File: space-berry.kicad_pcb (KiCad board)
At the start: 6 copper layers, 97 parts, among them J1 ARJM11C7-502-AB-ER2-T, Q1 SiS415DNT, Q2 TSM2302CX, U11 RTL8211F-CG, U12 K4A8G165WC-BCTD, U13 XCZU15EG-2FFVB1156E, U6 TLV75801PDBV, U7 TLV75801PDBV, U8 TLV75801PDBV, U9 TLV75801PDBV

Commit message: Stuff
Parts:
- removed J1: ARJM11C7-502-AB-ER2-T, lib:ARJM11C7-502-AB-ER2-T_ABR
- added R20: 22, Resistor_SMD:R_0402_1005Metric_Pad0.72x0.64mm_HandSolder, F.Cu at (61.6, 86.6)
- added R33: 22, Resistor_SMD:R_0402_1005Metric_Pad0.72x0.64mm_HandSolder, F.Cu at (61.6, 88.6)
- added R34: 22, Resistor_SMD:R_0402_1005Metric_Pad0.72x0.64mm_HandSolder, F.Cu at (61.6, 90.6)
- added R35: 22, Resistor_SMD:R_0402_1005Metric_Pad0.72x0.64mm_HandSolder, F.Cu at (61.6, 92.6)
- added R36: 4K7, Resistor_SMD:R_0402_1005Metric_Pad0.72x0.64mm_HandSolder, F.Cu at (61.6, 94.5)
- added R37: 4K7, Resistor_SMD:R_0402_1005Metric_Pad0.72x0.64mm_HandSolder, F.Cu at (61.6, 96.5)
- added R38: 4K7, Resistor_SMD:R_0402_1005Metric_Pad0.72x0.64mm_HandSolder, F.Cu at (64.8, 86.6)
- added R39: 4K7, Resistor_SMD:R_0402_1005Metric_Pad0.72x0.64mm_HandSolder, F.Cu at (64.8, 88.6)
- added R41: 4K7, Resistor_SMD:R_0402_1005Metric_Pad0.72x0.64mm_HandSolder, F.Cu at (64.8, 90.6)
- added R42: 4K7, Resistor_SMD:R_0402_1005Metric_Pad0.72x0.64mm_HandSolder, F.Cu at (64.8, 92.6)
- added R43: 4K7, Resistor_SMD:R_0402_1005Metric_Pad0.72x0.64mm_HandSolder, F.Cu at (64.8, 94.5)
- added R44: 4K7, Resistor_SMD:R_0402_1005Metric_Pad0.72x0.64mm_HandSolder, F.Cu at (64.8, 96.5)
- added R45: 22, Resistor_SMD:R_0402_1005Metric_Pad0.72x0.64mm_HandSolder, F.Cu at (68.1, 86.6)
- added R46: 22, Resistor_SMD:R_0402_1005Metric_Pad0.72x0.64mm_HandSolder, F.Cu at (68.1, 88.6)
- added R47: 22, Resistor_SMD:R_0402_1005Metric_Pad0.72x0.64mm_HandSolder, F.Cu at (68.1, 90.6)
- added R48: 22, Resistor_SMD:R_0402_1005Metric_Pad0.72x0.64mm_HandSolder, F.Cu at (68.1, 92.6)
- moved U11 9.92 mm to (73.5, 89.4)
- moved U12 8.24 mm to (136.8, 74.9)
- moved R23 5.93 mm to (154.8, 48.0), turned to 90 degrees
- moved R24 5.93 mm to (152.0, 53.2), turned to 0 degrees
- moved C28 4.25 mm to (118.4, 56.9), turned to -90 degrees
- moved R19 3.77 mm to (146.0, 74.8), turned to 90 degrees
- moved R27 2.02 mm to (116.9, 54.2), turned to 180 degrees
- moved R28 1.28 mm to (113.2, 54.2)
- moved C27 1.28 mm to (112.0, 56.9)
- moved U9 1.28 mm to (115.2, 56.9)
- moved U13 0.99 mm to (108.0, 81.1)
- turned C24 to -90 degrees
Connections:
- U11 pad 1: unconnected-(U11A-MDIP0-Pad1) -> ETH_TR1+
- U11 pad 10: unconnected-(U11A-MDIN3-Pad10) -> ETH_TR4-
- U11 pad 11: unconnected-(U11B-AVDD33-Pad11) -> (no net)
- U11 pad 15: unconnected-(U11A-TXD3-Pad15) -> Net-(U11A-TXD3)
- U11 pad 16: unconnected-(U11A-TXD2-Pad16) -> Net-(U11A-TXD2)
- U11 pad 17: unconnected-(U11A-TXD1-Pad17) -> Net-(U11A-TXD1)
- U11 pad 18: unconnected-(U11A-TXD0-Pad18) -> Net-(U11A-TXD0)
- U11 pad 2: unconnected-(U11A-MDIN0-Pad2) -> ETH_TR1-
- U11 pad 21: unconnected-(U11B-DVDD10-Pad21) -> (no net)
- U11 pad 22: unconnected-(U11A-RXD3/PHYAD0-Pad22) -> Net-(U11A-RXD3/PHYAD0)
- U11 pad 23: unconnected-(U11A-RXD2/PLLOFF-Pad23) -> Net-(U11A-RXD2/PLLOFF)
- U11 pad 24: unconnected-(U11A-RXD1/TXDLY-Pad24) -> Net-(U11A-RXD1/TXDLY)
- U11 pad 25: unconnected-(U11A-RXD0/RXDLY-Pad25) -> Net-(U11A-RXD0/RXDLY)
- U11 pad 28: unconnected-(U11B-DVDD_RG-Pad28) -> (no net)
- U11 pad 29: unconnected-(U11B-DVDD33-Pad29) -> (no net)
- U11 pad 3: unconnected-(U11B-AVDD10-Pad3) -> (no net)
- U11 pad 38: unconnected-(U11B-AVDD10-Pad38) -> (no net)
- U11 pad 4: unconnected-(U11A-MDIP1-Pad4) -> ETH_TR2+
- U11 pad 40: unconnected-(U11B-AVDD33-Pad40) -> (no net)
- U11 pad 41: unconnected-(U11B-GND-Pad41) -> (no net)
- U11 pad 5: unconnected-(U11A-MDIN1-Pad5) -> ETH_TR2-
- U11 pad 6: unconnected-(U11A-MDIP2-Pad6) -> ETH_TR3+
- U11 pad 7: unconnected-(U11A-MDIN2-Pad7) -> ETH_TR3-
- U11 pad 8: unconnected-(U11B-AVDD10-Pad8) -> (no net)
- U11 pad 9: unconnected-(U11A-MDIP3-Pad9) -> ETH_TR4+
- U13 pad A1: (no net) -> Net-(U13P-GND-PadA1)
- U13 pad A10: (no net) -> Net-(U13M-MGTAVCC_R-PadA10)
- U13 pad A2: (no net) -> Net-(U13P-GND-PadA1)
- U13 pad A30: (no net) -> unconnected-(U13M-MGTAVTTRCAL_L-PadA30)
- U13 pad A5: (no net) -> unconnected-(U13M-MGTAVTTRCAL_R-PadA5)
- U13 pad A9: (no net) -> Net-(U13P-GND-PadA1)
- U13 pad AA13: (no net) -> Net-(U13O-VCCINT_IO-PadAA13)
- U13 pad AA15: (no net) -> VCC_INT
- U13 pad AA17: (no net) -> VCC_INT
- U13 pad AA19: (no net) -> VCC_INT
- U13 pad AA21: (no net) -> Net-(U13N-VCC_PSINTLP-PadAA21)
- U13 pad AA22: (no net) -> unconnected-(U13N-VCC_PSBATT-PadAA22)
- U13 pad AA23: (no net) -> Net-(U13N-VCC_PSADC-PadAB25)
- U13 pad AA25: (no net) -> Net-(U13N-VCC_PSADC-PadAB25)
- U13 pad AA29: (no net) -> Net-(U13N-PS_MGTRAVCC-PadAA29)
- U13 pad AA9: (no net) -> unconnected-(U13P-VCCO_66-PadAA9)
- U13 pad AB13: (no net) -> Net-(U13O-VCCINT_IO-PadAA13)
- U13 pad AB14: (no net) -> Net-(U13N-VCCBRAM-PadAB14)
- U13 pad AB16: (no net) -> VCC_INT
- U13 pad AB18: (no net) -> VCC_INT
- U13 pad AB20: (no net) -> VCC_INT
- U13 pad AB21: (no net) -> Net-(U13N-VCC_PSINTLP-PadAA21)
- U13 pad AB23: (no net) -> Net-(U13N-VCC_PSINTLP-PadAA21)
- U13 pad AB25: (no net) -> Net-(U13N-VCC_PSADC-PadAB25)
- U13 pad AB32: (no net) -> Net-(U13N-PS_MGTRAVTT-PadAB32)
- U13 pad AC13: (no net) -> Net-(U13O-VCCINT_IO-PadAA13)
- U13 pad AC14: (no net) -> Net-(U13N-VCCBRAM-PadAB14)
- U13 pad AC15: (no net) -> VCC_INT
- U13 pad AC17: (no net) -> VCC_INT
- U13 pad AC19: (no net) -> VCC_INT
- U13 pad AC21: (no net) -> Net-(U13N-VCC_PSINTLP-PadAA21)
- U13 pad AC22: (no net) -> Net-(U13N-VCC_PSINTLP-PadAA21)
- U13 pad AC23: (no net) -> Net-(U13N-VCC_PSINTLP-PadAA21)
- U13 pad AC24: (no net) -> Net-(U13N-VCC_PSINTFP-PadAC24)
- U13 pad AC26: (no net) -> Net-(U13N-VCC_PSADC-PadAB25)
- U13 pad AD11: (no net) -> unconnected-(U13P-VREF_65-PadAD11)
- U13 pad AD12: (no net) -> unconnected-(U13P-VREF_66-PadAD12)
- U13 pad AD17: unconnected-(U13K-PS_MIO7-PadAD17) -> UART0_TX
- U13 pad AD18: unconnected-(U13K-PS_MIO20-PadAD18) -> SD_DATA7
- U13 pad AD20: unconnected-(U13K-PS_MIO22-PadAD20) -> SD_CLK
- U13 pad AD21: (no net) -> Net-(U13N-VCC_PSINTFP-PadAC24)
- U13 pad AD22: (no net) -> Net-(U13N-VCC_PSINTFP-PadAC24)
- U13 pad AD24: (no net) -> Net-(U13N-VCC_PSINTFP_DDR-PadAD24)
- U13 pad AD25: (no net) -> Net-(U13N-VCC_PSINTFP-PadAC24)
- U13 pad AD26: (no net) -> Net-(U13N-VCC_PSINTFP-PadAC24)
- U13 pad AD8: (no net) -> unconnected-(U13P-VCCO_65-PadAD8)
- U13 pad AE16: (no net) -> Net-(U13P-VCCO_PSIO0_500-PadAE16)
- U13 pad AE17: unconnected-(U13K-PS_MIO8-PadAE17) -> UART1_RX
- U13 pad AE18: unconnected-(U13K-PS_MIO18-PadAE18) -> SD_DATA5
- U13 pad AE22: (no net) -> Net-(U13N-VCC_PSINTFP-PadAC24)
- U13 pad AE23: (no net) -> Net-(U13N-VCC_PSINTFP-PadAC24)
- U13 pad AE24: (no net) -> Net-(U13N-VCC_PSINTFP_DDR-PadAD24)
- U13 pad AE25: (no net) -> Net-(U13N-VCC_PSINTFP_DDR-PadAD24)
- U13 pad AF14: (no net) -> unconnected-(U13P-VCCO_44-PadAF14)
- U13 pad AF18: unconnected-(U13K-PS_MIO21-PadAF18) -> SD_CMD
- U13 pad AF26: (no net) -> unconnected-(U13M-NC-PadAF26)
- U13 pad AF27: (no net) -> unconnected-(U13M-NC-PadAF27)
- U13 pad AF9: (no net) -> unconnected-(U13P-VCCO_65-PadAF9)
- U13 pad AG17: (no net) -> Net-(U13P-VCCO_PSIO0_500-PadAE16)
- U13 pad AG27: (no net) -> Net-(U13P-VCCO_PSDDR_504-PadAG27)
- U13 pad AG7: (no net) -> unconnected-(U13P-VCCO_65-PadAG7)
- U13 pad AJ11: (no net) -> unconnected-(U13P-VREF_64-PadAJ11)
- U13 pad AJ13: (no net) -> unconnected-(U13P-VCCO_44-PadAJ13)
- U13 pad AJ24: (no net) -> Net-(U13P-VCCO_PSDDR_504-PadAG27)
- U13 pad AJ28: (no net) -> Net-(U13P-VCCO_PSDDR_504-PadAG27)
- U13 pad AJ8: (no net) -> unconnected-(U13P-VCCO_64-PadAJ8)
- U13 pad AK11: (no net) -> unconnected-(U13P-VCCO_64-PadAK11)
- U13 pad AK16: (no net) -> Net-(U13P-VCCO_PSIO0_500-PadAE16)
- U13 pad AK17: unconnected-(U13K-PS_MIO13-PadAK17) -> SD_DATA0
- U13 pad AL15: unconnected-(U13K-PS_MIO6-PadAL15) -> UART0_RX
- U13 pad AL16: unconnected-(U13K-PS_MIO14-PadAL16) -> SD_DATA1
- U13 pad AL17: unconnected-(U13K-PS_MIO19-PadAL17) -> SD_DATA6
- U13 pad AL24: (no net) -> Net-(U13P-VCCO_PSDDR_504-PadAG27)
- U13 pad AL29: (no net) -> Net-(U13P-VCCO_PSDDR_504-PadAG27)
- U13 pad AL9: (no net) -> unconnected-(U13P-VCCO_64-PadAL9)
- U13 pad AM16: unconnected-(U13K-PS_MIO16-PadAM16) -> SD_DATA3
- U13 pad AN16: unconnected-(U13K-PS_MIO15-PadAN16) -> SD_DATA2
- U13 pad AN25: (no net) -> Net-(U13P-VCCO_PSDDR_504-PadAG27)
- U13 pad AN30: (no net) -> Net-(U13P-VCCO_PSDDR_504-PadAG27)
- U13 pad AP15: unconnected-(U13K-PS_MIO9-PadAP15) -> UART1_TX
- U13 pad AP16: unconnected-(U13K-PS_MIO17-PadAP16) -> SD_DATA4
- U13 pad B3: (no net) -> Net-(U13M-MGTAVTT_R-PadB3)
- U13 pad B31: (no net) -> Net-(U13M-MGTAVTT_L-PadB31)
- U13 pad B4: (no net) -> Net-(U13P-GND-PadA1)
- U13 pad B8: (no net) -> Net-(U13M-MGTAVCC_R-PadA10)
- U13 pad C29: (no net) -> Net-(U13M-MGTAVTT_L-PadB31)
- U13 pad C6: (no net) -> Net-(U13M-MGTAVCC_R-PadA10)
- U13 pad D23: (no net) -> Net-(U13P-VCCO_PSIO2_502-PadD23)
- U13 pad D32: (no net) -> Net-(U13M-MGTAVTT_L-PadB31)
- U13 pad D4: (no net) -> Net-(U13M-MGTAVTT_R-PadB3)
- U13 pad D7: (no net) -> Net-(U13M-MGTAVCC_R-PadA10)
- U13 pad E16: (no net) -> unconnected-(U13P-VCCO_49-PadE16)
- U13 pad E21: (no net) -> unconnected-(U13P-VCCO_47-PadE21)
- U13 pad E30: (no net) -> Net-(U13M-MGTAVTT_L-PadB31)
- U13 pad E5: (no net) -> Net-(U13M-MGTAVCC_R-PadA10)
- U13 pad F14: (no net) -> unconnected-(U13P-VCCO_49-PadF14)
- U13 pad F24: (no net) -> Net-(U13P-VCCO_PSIO2_502-PadD23)
- U13 pad F28: (no net) -> Net-(U13M-MGTAVCC_L-PadF28)
- U13 pad F3: (no net) -> Net-(U13M-MGTAVTT_R-PadB3)
- U13 pad F31: (no net) -> Net-(U13M-MGTAVTT_L-PadB31)
- U13 pad F8: (no net) -> Net-(U13M-MGTVCCAUX_R-PadF8)
- U13 pad G12: (no net) -> unconnected-(U13P-VCCO_50-PadG12)
- U13 pad G17: (no net) -> unconnected-(U13P-VCCO_48-PadG17)
- U13 pad G22: (no net) -> Net-(U13P-VCCO_PSIO2_502-PadD23)
- U13 pad G29: (no net) -> Net-(U13M-MGTAVCC_L-PadF28)
- U13 pad G6: (no net) -> Net-(U13M-MGTAVCC_R-PadA10)
- U13 pad H20: (no net) -> unconnected-(U13P-VCCO_47-PadH20)
- U13 pad H27: (no net) -> Net-(U13M-MGTAVCC_L-PadF28)
- U13 pad H32: (no net) -> Net-(U13M-MGTAVTT_L-PadB31)
- U13 pad H4: (no net) -> Net-(U13M-MGTAVTT_R-PadB3)
- U13 pad H7: (no net) -> Net-(U13M-MGTVCCAUX_R-PadF8)
- U13 pad J13: (no net) -> unconnected-(U13P-VCCO_50-PadJ13)
- U13 pad J18: (no net) -> unconnected-(U13P-VCCO_48-PadJ18)
- U13 pad J24: unconnected-(U13K-PS_MIO41-PadJ24) -> ETH_TXD2
- U13 pad J25: unconnected-(U13K-PS_MIO46-PadJ25) -> ETH_RXD3
- U13 pad J30: (no net) -> Net-(U13M-MGTAVTT_L-PadB31)
- U13 pad J5: (no net) -> Net-(U13M-MGTAVTT_R-PadB3)
- U13 pad K24: unconnected-(U13K-PS_MIO43-PadK24) -> ETH_RXD0
- U13 pad K28: (no net) -> Net-(U13M-MGTVCCAUX_L-PadK28)
- U13 pad K3: (no net) -> Net-(U13M-MGTAVTT_R-PadB3)
- U13 pad K31: (no net) -> Net-(U13M-MGTAVTT_L-PadB31)
- U13 pad K8: (no net) -> Net-(U13M-MGTAVCC_R-PadA10)
- U13 pad L23: unconnected-(U13K-PS_MIO38-PadL23) -> ETH_CLK
- U13 pad L24: (no net) -> Net-(U13P-VCCO_PSIO1_501-PadL24)
- U13 pad L29: (no net) -> Net-(U13M-MGTAVCC_L-PadF28)
- U13 pad L6: (no net) -> Net-(U13M-MGTAVTT_R-PadB3)
- U13 pad M16: (no net) -> VCC_INT
- U13 pad M18: (no net) -> VCC_INT
- U13 pad M20: (no net) -> VCC_INT
- U13 pad M22: (no net) -> Net-(U13P-VCCO_PSIO1_501-PadL24)
- U13 pad M23: unconnected-(U13K-PS_MIO40-PadM23) -> ETH_TXD1
- U13 pad M24: unconnected-(U13K-PS_MIO42-PadM24) -> ETH_TXD3
- U13 pad M27: (no net) -> Net-(U13M-MGTVCCAUX_L-PadK28)
- U13 pad M32: (no net) -> Net-(U13M-MGTAVTT_L-PadB31)
- U13 pad M4: (no net) -> Net-(U13M-MGTAVTT_R-PadB3)
- U13 pad N14: (no net) -> unconnected-(U13P-VREF_67-PadN14)
- U13 pad N15: (no net) -> VCC_INT
- U13 pad N17: (no net) -> VCC_INT
- U13 pad N19: (no net) -> VCC_INT
- U13 pad N23: unconnected-(U13K-PS_MIO39-PadN23) -> ETH_TXD0
- U13 pad N24: unconnected-(U13K-PS_MIO44-PadN24) -> ETH_RXD1
- U13 pad N30: (no net) -> Net-(U13M-MGTAVTT_L-PadB31)
- U13 pad N5: (no net) -> Net-(U13M-MGTAVTT_R-PadB3)
- U13 pad P14: (no net) -> VCC_INT
- U13 pad P16: (no net) -> VCC_INT
- U13 pad P18: (no net) -> VCC_INT
- U13 pad P20: (no net) -> VCC_INT
- U13 pad P24: unconnected-(U13K-PS_MIO45-PadP24) -> ETH_RXD2
- U13 pad P28: (no net) -> Net-(U13M-MGTAVCC_L-PadF28)
- U13 pad P3: (no net) -> Net-(U13M-MGTAVTT_R-PadB3)
- U13 pad P31: (no net) -> Net-(U13M-MGTAVTT_L-PadB31)
- U13 pad P8: (no net) -> unconnected-(U13P-VCCO_67-PadP8)
- U13 pad R15: (no net) -> VCC_INT
- U13 pad R17: (no net) -> VCC_INT
- U13 pad R19: (no net) -> VCC_INT
- U13 pad R29: (no net) -> Net-(U13M-MGTAVCC_L-PadF28)
- U13 pad T14: (no net) -> Net-(U13N-VCCAUX-PadT14)
- U13 pad T16: (no net) -> VCC_INT
- U13 pad T18: (no net) -> unconnected-(U13N-VCCADC-PadT18)
- U13 pad T20: (no net) -> VCC_INT
- U13 pad T24: (no net) -> Net-(U13P-VCCO_PSIO3_503-PadT24)
- U13 pad T9: (no net) -> unconnected-(U13P-VCCO_67-PadT9)
- U13 pad U13: (no net) -> Net-(U13N-VCCAUX_IO-PadU13)
- U13 pad U14: (no net) -> Net-(U13N-VCCAUX-PadT14)
- U13 pad U15: (no net) -> VCC_INT
- U13 pad U17: (no net) -> unconnected-(U13P-VREFN-PadU17)
- U13 pad U19: (no net) -> VCC_INT
- U13 pad U22: (no net) -> Net-(U13P-VCCO_PSIO3_503-PadT24)
- U13 pad U7: (no net) -> unconnected-(U13P-VCCO_67-PadU7)
- U13 pad V13: (no net) -> Net-(U13N-VCCAUX_IO-PadU13)
- U13 pad V14: (no net) -> Net-(U13N-VCCAUX_IO-PadU13)
- U13 pad V16: (no net) -> VCC_INT
- U13 pad V18: (no net) -> unconnected-(U13P-VREFP-PadV18)
- U13 pad V20: (no net) -> VCC_INT
- U13 pad V28: (no net) -> Net-(U13N-PS_MGTRAVCC-PadAA29)
- U13 pad V32: (no net) -> Net-(U13N-PS_MGTRAVTT-PadAB32)
- U13 pad W14: (no net) -> Net-(U13N-VCCBRAM-PadAB14)
- U13 pad W15: (no net) -> VCC_INT
- U13 pad W19: (no net) -> VCC_INT
- U13 pad W22: (no net) -> Net-(U13N-VCC_PSPLL-PadW22)
- U13 pad W24: (no net) -> Net-(U13N-VCC_PSPLL-PadW22)
- U13 pad W25: (no net) -> Net-(U13N-VCC_PSPLL-PadW22)
- U13 pad W30: (no net) -> Net-(U13N-PS_MGTRAVCC-PadAA29)
- U13 pad W8: (no net) -> unconnected-(U13P-VCCO_66-PadW8)
- U13 pad Y11: (no net) -> unconnected-(U13P-VCCO_66-PadY11)
- U13 pad Y13: (no net) -> Net-(U13O-VCCINT_IO-PadAA13)
- U13 pad Y14: (no net) -> Net-(U13N-VCCBRAM-PadAB14)
- U13 pad Y16: (no net) -> VCC_INT
- U13 pad Y18: (no net) -> VCC_INT
- U13 pad Y20: (no net) -> VCC_INT
- U13 pad Y22: (no net) -> Net-(U13N-VCC_PSADC-PadAB25)
- U13 pad Y23: (no net) -> Net-(U13N-VCC_PSADC-PadAB25)
- U13 pad Y24: (no net) -> Net-(U13N-VCC_PSDDR_PLL-PadY24)
- U13 pad Y25: (no net) -> Net-(U13N-VCC_PSDDR_PLL-PadY24)
- U13 pad Y27: (no net) -> Net-(U13N-PS_MGTRAVCC-PadAA29)
- U13 pad Y31: (no net) -> Net-(U13N-PS_MGTRAVTT-PadAB32)
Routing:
- net VCC_INT: track 0.00 -> 31.2 mm, vias 0 -> 2
- net GND: track 212.1 -> 192.6 mm, vias 22 -> 23
- net Net-(U7-FB): track 0.00 -> 16.9 mm
- net 3V3: track 0.00 -> 13.0 mm
- net Net-(U8-FB): track 0.00 -> 8.43 mm
- net Net-(U6-FB): track 0.00 -> 8.43 mm
- net 0V85_LDO: track 0.00 -> 7.76 mm
- net Net-(U13N-VCC_PSINTLP-PadAA21): track 0.00 -> 5.00 mm
- net 1V8: track 0.00 -> 4.10 mm
- net 1V8_LDO: track 0.00 -> 3.88 mm
- net 2V5_LDO: track 0.00 -> 3.88 mm
- net DDR_CK-: track 0.57 -> 0.00 mm, vias 2 -> 1
- net DDR_CK+: track 0.57 -> 0.00 mm, vias 2 -> 1
- net Net-(U4-PG): vias 4 -> 3
- net Net-(U4-EN): vias 4 -> 3
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- added copper zone on F.Cu, net Net-(Q1-D)

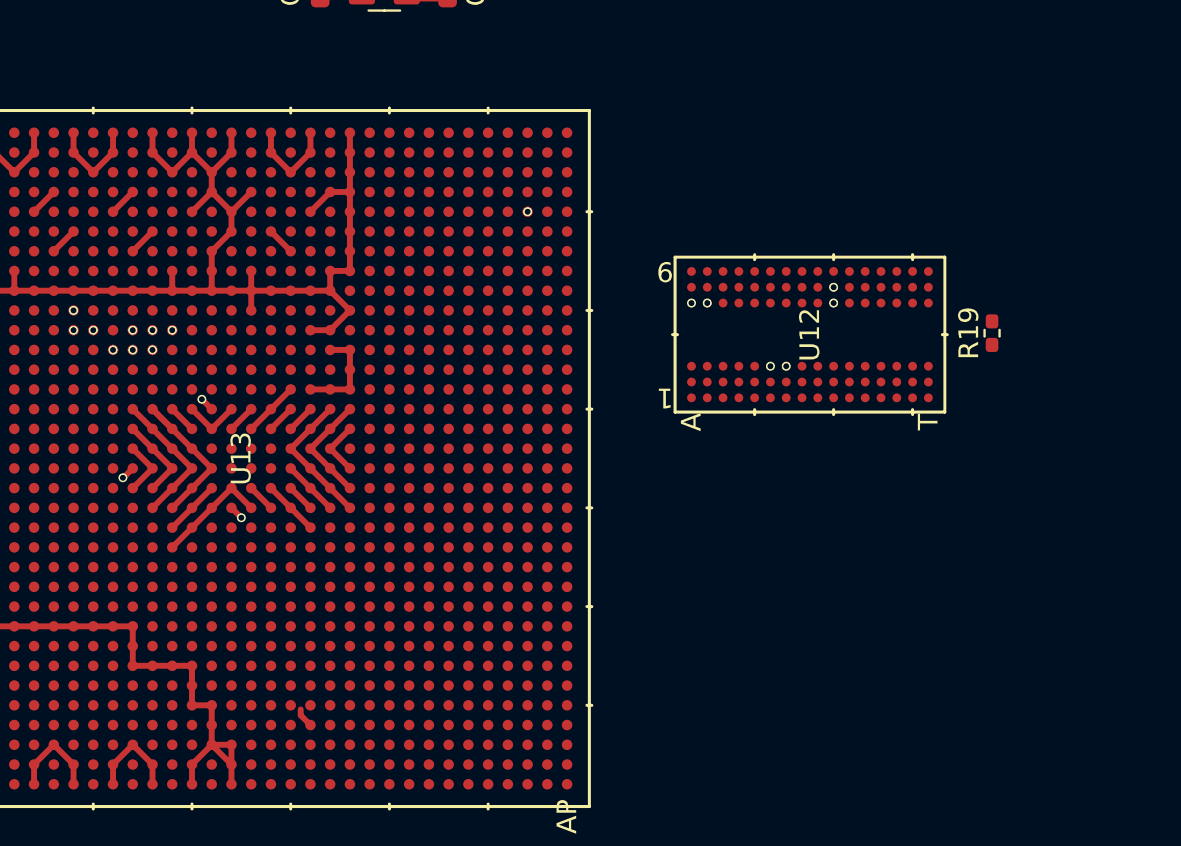
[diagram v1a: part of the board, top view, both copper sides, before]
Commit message: DDR4 data lines
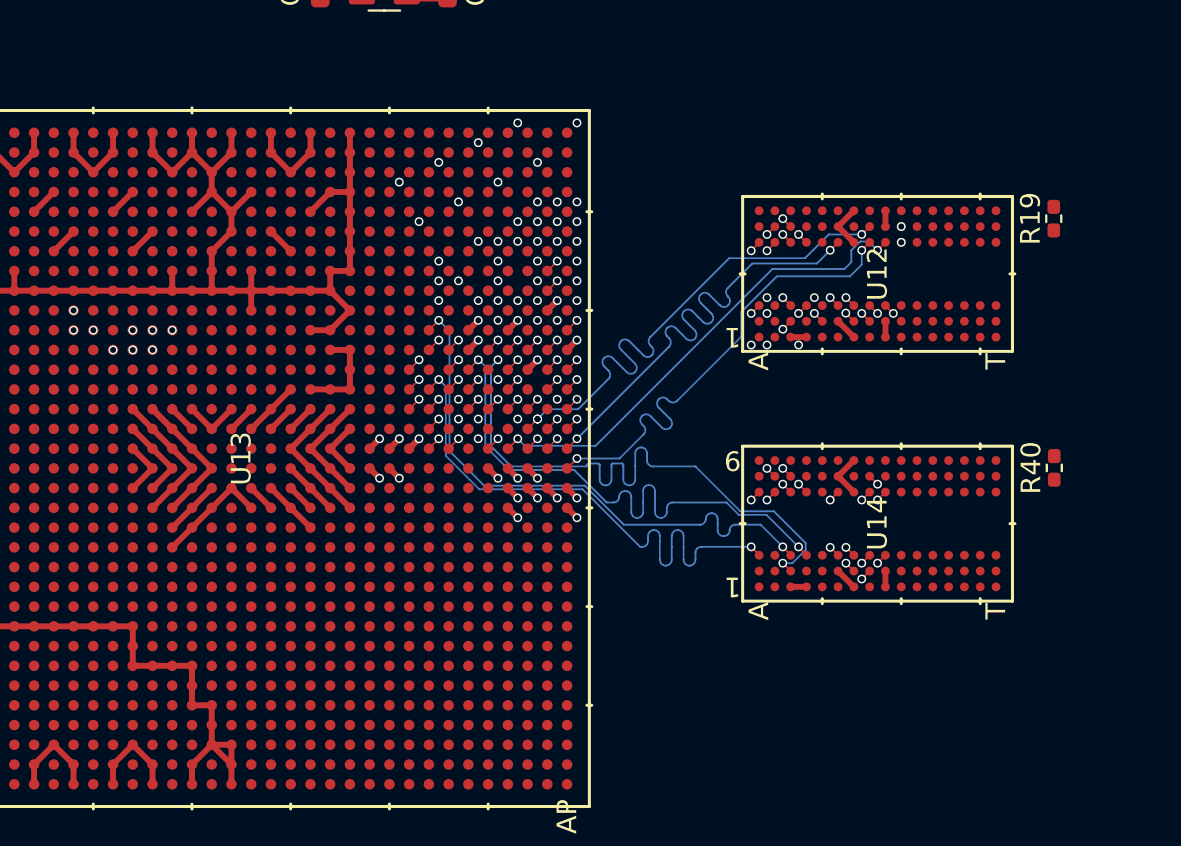
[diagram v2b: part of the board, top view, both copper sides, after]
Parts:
- added R40: 499, Resistor_SMD:R_0402_1005Metric_Pad0.72x0.64mm_HandSolder, F.Cu at (149.2, 81.6)
- added U14: K4A8G165WC-BCTD, lib:FBGA96X16_7P5X13P3_SAM, F.Cu at (140.2, 84.5)
- moved R19 6.59 mm to (149.2, 69.0)
- moved U12 4.60 mm to (140.2, 71.8)
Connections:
- U13 pad AG18: unconnected-(U13J-PS_DDR_DQ23-PadAG18) -> DDR_BY_L23
- U13 pad AG19: unconnected-(U13J-PS_DDR_DQ22-PadAG19) -> DDR_BY_L22
- U13 pad AG20: unconnected-(U13J-PS_DDR_DQ20-PadAG20) -> DDR_BY_L20
- U13 pad AG21: unconnected-(U13J-PS_DDR_DQ24-PadAG21) -> DDR_BY_U24
- U13 pad AG23: unconnected-(U13J-PS_DDR_DQ27-PadAG23) -> DDR_BY_U27
- U13 pad AG24: unconnected-(U13J-PS_DDR_DQ26-PadAG24) -> DDR_BY_U26
- U13 pad AH18: unconnected-(U13J-PS_DDR_DQ21-PadAH18) -> DDR_BY_L21
- U13 pad AH19: unconnected-(U13K-PS_DDR_DQS_P2-PadAH19) -> DDR_DQS2+
- U13 pad AH21: unconnected-(U13J-PS_DDR_DQ25-PadAH21) -> DDR_BY_U25
- U13 pad AH22: unconnected-(U13K-PS_DDR_DQS_P3-PadAH22) -> DDR_DQS3+
- U13 pad AH23: unconnected-(U13K-PS_DDR_DQS_N3-PadAH23) -> DDR_DQS3-
- U13 pad AJ19: unconnected-(U13K-PS_DDR_DQS_N2-PadAJ19) -> DDR_DQS2-
- U13 pad AJ20: unconnected-(U13J-PS_DDR_DQ18-PadAJ20) -> DDR_BY_L18
- U13 pad AJ21: unconnected-(U13J-PS_DDR_DQ29-PadAJ21) -> DDR_BY_U29
- U13 pad AJ22: unconnected-(U13J-PS_DDR_DQ30-PadAJ22) -> DDR_BY_U30
- U13 pad AK18: unconnected-(U13J-PS_DDR_DQ19-PadAK18) -> DDR_BY_L19
- U13 pad AK20: unconnected-(U13J-PS_DDR_DQ17-PadAK20) -> DDR_BY_L17
- U13 pad AK22: unconnected-(U13J-PS_DDR_DQ28-PadAK22) -> DDR_BY_U28
- U13 pad AK23: unconnected-(U13J-PS_DDR_DQ31-PadAK23) -> DDR_BY_U31
- U13 pad AL20: unconnected-(U13J-PS_DDR_DQ16-PadAL20) -> DDR_BY_L16
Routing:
- net DDR_BY_L22: track 0.00 -> 30.7 mm, vias 0 -> 2
- net DDR_BY_L20: track 0.00 -> 30.7 mm, vias 0 -> 2
- net DDR_DQS2+: track 0.00 -> 30.7 mm, vias 0 -> 2
- net DDR_BY_L18: track 0.00 -> 30.6 mm, vias 0 -> 2
- net DDR_BY_L16: track 0.00 -> 30.6 mm, vias 0 -> 2
- net DDR_DQS2-: track 0.00 -> 30.6 mm, vias 0 -> 2
- net DDR_BY_U28: track 0.00 -> 30.0 mm, vias 0 -> 2
- net DDR_DQS3+: track 0.00 -> 29.7 mm, vias 0 -> 2
- net DDR_DQS3-: track 0.00 -> 29.7 mm, vias 0 -> 2
- net DDR_BY_L21: track 0.00 -> 29.5 mm, vias 0 -> 2
- net DDR_BY_L23: track 0.00 -> 29.5 mm, vias 0 -> 2
- net DDR_BY_U31: track 0.00 -> 29.4 mm, vias 0 -> 2
- net DDR_BY_U27: track 0.00 -> 29.4 mm, vias 0 -> 2
- net DDR_BY_L19: track 0.00 -> 29.4 mm, vias 0 -> 2
- net DDR_BY_U25: track 0.00 -> 29.4 mm, vias 0 -> 2
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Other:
- copper layers 6 -> 8

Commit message: DDR4 finish
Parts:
- added C19: 100nF, Capacitor_SMD:C_0402_1005Metric, F.Cu at (145.9, 76.9)
- added C20: 100nF, Capacitor_SMD:C_0402_1005Metric, F.Cu at (140.4, 66.9)
- added C29: 100nF, Capacitor_SMD:C_0402_1005Metric, F.Cu at (135.0, 66.9)
- added C30: 100nF, Capacitor_SMD:C_0402_1005Metric, F.Cu at (141.1, 76.9)
- added C31: 100nF, Capacitor_SMD:C_0402_1005Metric, F.Cu at (135.0, 79.5)
- added C32: 100nF, Capacitor_SMD:C_0402_1005Metric, F.Cu at (140.4, 79.5)
- added C33: 100nF, Capacitor_SMD:C_0402_1005Metric, F.Cu at (145.9, 89.8)
- added C34: 100nF, Capacitor_SMD:C_0402_1005Metric, F.Cu at (141.1, 89.8)
- added C35: 100nF, Capacitor_SMD:C_0402_1005Metric, F.Cu at (145.9, 66.9)
- added C36: 4.7uF, Capacitor_SMD:C_0603_1608Metric, F.Cu at (135.8, 77.1)
- added C37: 4.7uF, Capacitor_SMD:C_0603_1608Metric, F.Cu at (135.8, 89.8)
- added C38: 100nF, Capacitor_SMD:C_0402_1005Metric, F.Cu at (145.9, 79.6)
- added R49: 240, Resistor_SMD:R_0402_1005Metric, F.Cu at (137.7, 79.5)
- added R50: 240, Resistor_SMD:R_0402_1005Metric, F.Cu at (137.8, 66.9)
- moved C21 14.7 mm to (151.1, 46.6)
- moved C22 14.7 mm to (153.8, 51.6)
- moved R21 14.7 mm to (153.8, 47.9)
- moved R22 14.7 mm to (151.0, 53.1)
- moved U8 14.7 mm to (151.0, 49.9)
- moved C27 14.4 mm to (97.6, 58.0)
- moved C28 14.4 mm to (104.1, 58.0)
- moved R27 14.4 mm to (102.6, 55.2)
- moved R28 14.4 mm to (98.9, 55.2)
- moved U9 14.4 mm to (100.9, 58.0)
- moved C23 7.95 mm to (144.1, 46.8)
- moved C24 7.95 mm to (146.8, 51.8)
- moved C25 7.95 mm to (136.3, 46.8)
- moved C26 7.95 mm to (139.0, 51.7)
- moved R23 7.95 mm to (146.8, 48.0)
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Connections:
- C7 pad 1: Net-(C7-Pad1) -> 1V2
- C8 pad 1: Net-(C7-Pad1) -> 1V2
- TP7 pad 1: Net-(C7-Pad1) -> 1V2
- U12 pad B1: 2V5 -> 2V5_LDO
- U12 pad F9: unconnected-(U12B-ZQ-PadF9) -> Net-(U12B-ZQ)
- U12 pad M1: unconnected-(U12B-VREFCA-PadM1) -> DDR_VREF
- U12 pad R9: 2V5 -> 2V5_LDO
- U14 pad B1: 2V5 -> 2V5_LDO
- U14 pad F9: unconnected-(U14B-ZQ-PadF9) -> Net-(U14B-ZQ)
- U14 pad M1: unconnected-(U14B-VREFCA-PadM1) -> DDR_VREF
- U14 pad R9: 2V5 -> 2V5_LDO
- U3 pad 17: Net-(C7-Pad1) -> 1V2
- U3 pad 18: Net-(C7-Pad1) -> 1V2
- U3 pad 20: Net-(C7-Pad1) -> 1V2
- U3 pad 21: Net-(C7-Pad1) -> 1V2
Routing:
- net 2V5_LDO: track 3.88 -> 87.6 mm
- net DDR_A13: track 0.00 -> 72.4 mm, vias 1 -> 3
- net 1V2: track 10.8 -> 74.1 mm, vias 3 -> 24
- net DDR_A7: track 0.00 -> 60.6 mm, vias 1 -> 3
- net DDR_A5: track 0.00 -> 58.2 mm, vias 1 -> 3
- net DDR_A16: track 0.00 -> 58.1 mm, vias 1 -> 3
- net DDR_CKE: track 0.00 -> 58.0 mm, vias 1 -> 3
- net DDR_ACT: track 0.00 -> 57.5 mm, vias 1 -> 3
- net DDR_A9: track 0.00 -> 57.3 mm, vias 1 -> 3
- net DDR_A12: track 0.00 -> 57.1 mm, vias 1 -> 3
- net DDR_A3: track 0.00 -> 57.1 mm, vias 1 -> 3
- net DDR_A1: track 0.00 -> 57.1 mm, vias 1 -> 3
- net DDR_CS: track 0.00 -> 57.0 mm, vias 1 -> 3
- net DDR_A2: track 0.00 -> 57.0 mm, vias 1 -> 3
- net DDR_A15: track 0.00 -> 56.9 mm, vias 1 -> 3
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- added copper zone on F.Cu, net 1V2
- added copper zone on In3.Cu, net 1V2
- removed copper zone on F.Cu, net Net-(C7-Pad1)
